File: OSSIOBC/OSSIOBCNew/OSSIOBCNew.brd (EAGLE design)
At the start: 94 x 94 mm, 151 parts, among them Q2 NX-3215, U1 PCA9548APWR, U10 MAX6369, U11 OPA4347, U12 TPS73233, U13 SN65HVD11QD, U14 LTC4411, U16 DS3231-L, U17 FM24V02-G, U18 TMP101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

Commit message: New OBC schematic / board file ok
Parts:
- removed C35: 1uF 0805, OSSI:C0805(2012)
- removed U12: TPS73233, OSSI:SOT23-5DBV
- added C42: 10uF, LDO Tantal 16V, OSSI:C1206(3216)-A
- added R75, R76, R77: 0, OSSI:R0603(1608)
- added U$1: OSSILOGORECT, OSSI:OSSILOGORECT1005
- added U15: MCP1700_SOT23, OSSI:SOT23
- C34: value 1uF 0805 -> 10uF, LDO Tantal 16V; device OSSI:C0805(2012) -> OSSI:C1206(3216)-A
- U9: value ADR127BUJZ-REEL7 -> ADR121
- moved R5 29.6 mm to (43.2, 19.0)
- moved R72 29.3 mm to (44.6, 19.0)
- moved C34 7.91 mm to (63.8, 80.9)
- moved R1 2.27 mm to (67.8, 85.0), turned to 0 degrees
- moved C3 1.38 mm to (66.1, 81.8)
- moved R29 0.12 mm to (41.5, 19.0)
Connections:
- new net N$59: C42.2, R75.1
- new net N$62: R76.1, U5.49
- new net N$64: R77.1, U5.50
- net 3.3VOBC: now also C42.1, U15.2; no longer C34.1, R5.2, R72.2, U12.5
- net 3.3VOBC_I2C: now also R5.2, R72.2
- net GND: now also R75.2, U15.1; no longer C35.2, U12.2
- net MUX_A0: now also R76.2; no longer U5.49
- net MUX_A1: now also R77.2; no longer U5.50
- net N$666: now also C34.1, U15.3; no longer C35.1, U12.1, U12.3
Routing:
- net BAT_TEMP: track 0.00 -> 71.2 mm, vias 0 -> 3
- net SUPERCAP_TEMP: track 0.00 -> 69.6 mm, vias 0 -> 3
- net 3.3VOBC: track 529.4 -> 520.6 mm, vias 20 -> 19
- net MUX_A0: track 36.8 -> 29.4 mm
- net N$666: track 15.2 -> 8.95 mm
- net 3.3VOBC_I2C: track 45.1 -> 50.1 mm
- net N$62: track 0.00 -> 4.83 mm
- net MUX_A1: track 33.5 -> 28.8 mm
- net GND: track 152.4 -> 155.7 mm
- net SC_-PFO: track 89.2 -> 86.0 mm
- net N$64: track 0.00 -> 3.11 mm
- net ADC1: track 28.2 -> 30.3 mm
- net SCOUT_-PG: track 88.9 -> 86.9 mm, vias 1 -> 2
- net N$59: track 0.00 -> 1.77 mm
- net VEXT: track 7.66 -> 8.91 mm
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
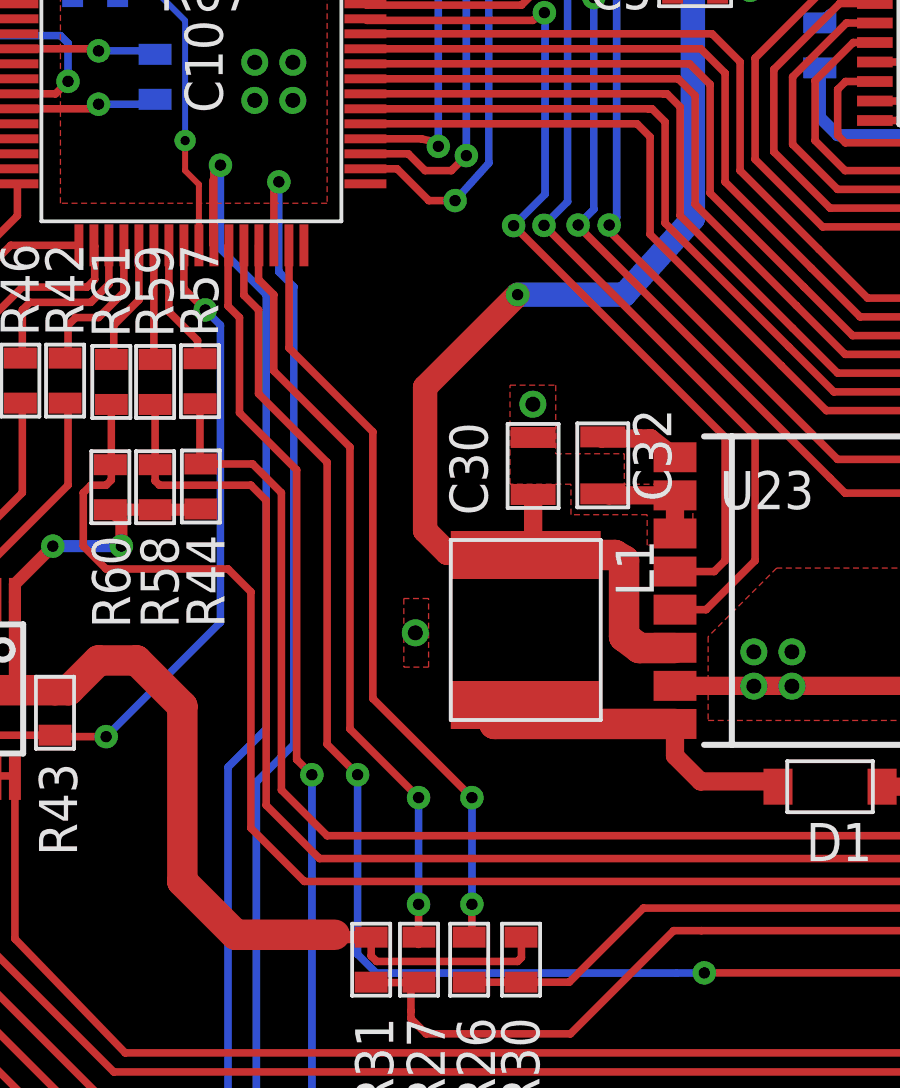
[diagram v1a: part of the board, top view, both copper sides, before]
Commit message: OSSI OBC New Gerber file added
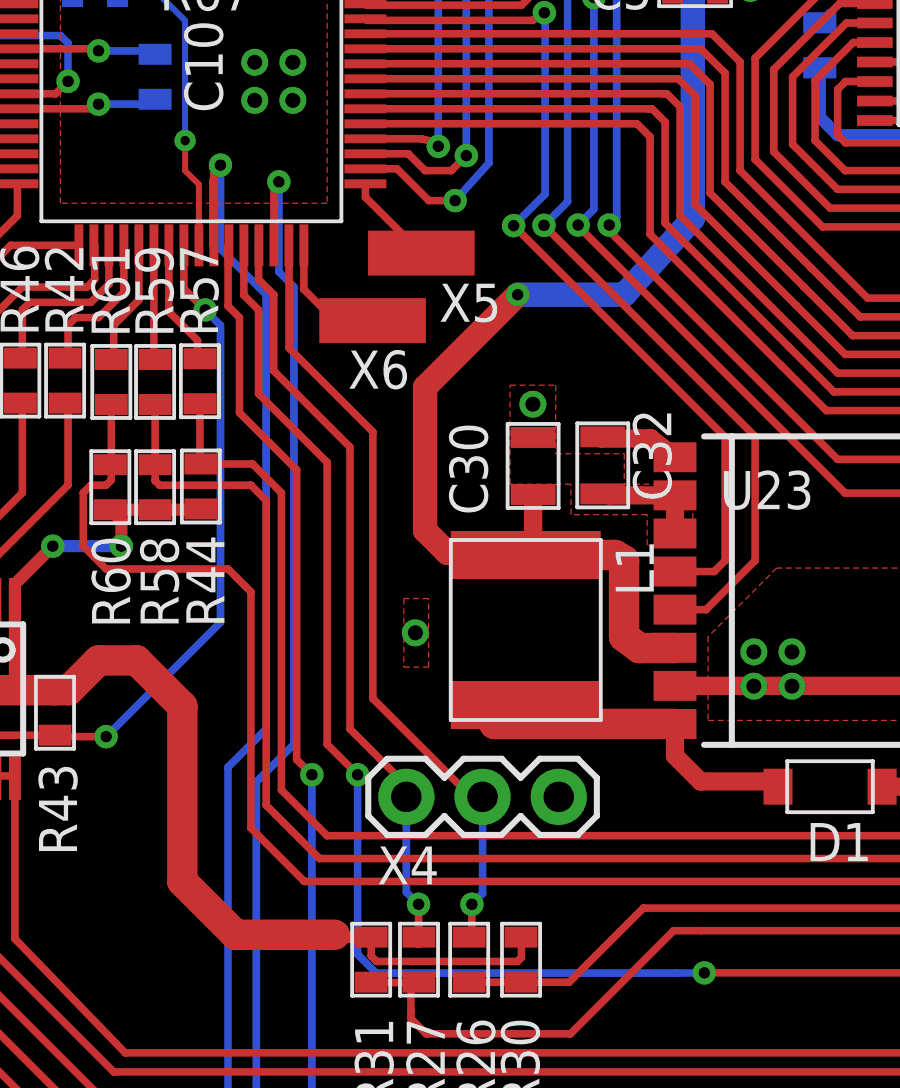
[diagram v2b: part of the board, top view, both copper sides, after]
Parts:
- added X4: (no value), OSSI:1X03
- added X5, X6: P-PAD-S, OSSI:P-PAD-S
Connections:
- new net I2C_SCL_TP: R26.2, U5.31, X4.2
- new net I2C_SDA_TP: R27.2, U5.29, X4.1
- net GND: now also X4.3
- net N$60: now also U5.33, X5.1; no longer R27.2, U5.29
- net N$61: now also U5.32, X6.1; no longer R26.2, U5.31
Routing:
- net I2C_SCL_TP: track 0.00 -> 26.5 mm, vias 0 -> 1
- net I2C_SDA_TP: track 0.00 -> 25.8 mm, vias 0 -> 1
- net N$60: track 25.8 -> 3.08 mm, vias 2 -> 0
- net N$61: track 25.9 -> 4.19 mm, vias 2 -> 0
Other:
- board text added: "A"
- board text added: "B"
- board text added: "GND"
- board text added: "LED"
- board text added: "SCL"
- board text added: "SDA"
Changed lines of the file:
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@@
 <layer number="19" name="Unrouted" color="6" fill="1" visible="yes" active="yes"/>
 <layer number="20" name="Dimension" color="15" fill="1" visible="yes" active="yes"/>
-<layer number="21" name="tPlace" color="7" fill="1" visible="yes" active="yes"/>
-<layer number="22" name="bPlace" color="7" fill="1" visible="yes" active="yes"/>
-<layer number="23" name="tOrigins" color="15" fill="1" visible="yes" active="yes"/>
-<layer number="24" name="bOrigins" color="15" fill="1" visible="yes" active="yes"/>
-<layer number="25" name="tNames" color="7" fill="1" visible="yes" active="yes"/>
-<layer number="26" name="bNames" color="7" fill="1" visible="yes" active="yes"/>
+<layer number="21" name="tPlace" color="7" fill="1" visible="no" active="yes"/>
+<layer number="22" name="bPlace" color="7" fill="1" visible="no" active="yes"/>
+<layer number="23" name="tOrigins" color="15" fill="1" visible="no" active="yes"/>
+<layer number="24" name="bOrigins" color="15" fill="1" visible="no" active="yes"/>
+<layer number="25" name="tNames" color="7" fill="1" visible="no" active="yes"/>
+<layer number="26" name="bNames" color="7" fill="1" visible="no" active="yes"/>
 <layer number="27" name="tValues" color="7" fill="1" visible="no" active="yes"/>
 <layer number="28" name="bValues" color="7" fill="1" visible="no" active="yes"/>
@@
 <layer number="46" name="Milling" color="3" fill="1" visible="no" active="yes"/>
 <layer number="47" name="Measures" color="7" fill="1" visible="no" active="yes"/>
-<layer number="48" name="Document" color="7" fill="1" visible="no" active="yes"/>
+<layer number="48" name="Document" color="7" fill="1" visible="yes" active="yes"/>
 <layer number="49" name="Reference" color="7" fill="1" visible="no" active="yes"/>
 <layer number="50" name="dxf" color="7" fill="1" visible="no" active="no"/>
-<layer number="51" name="tDocu" color="7" fill="1" visible="yes" active="yes"/>
-<layer number="52" name="bDocu" color="7" fill="1" visible="yes" active="yes"/>
+<layer number="51" name="tDocu" color="7" fill="1" visible="no" active="yes"/>
+<layer number="52" name="bDocu" color="7" fill="1" visible="no" active="yes"/>
 <layer number="53" name="tGND_GNDA" color="7" fill="9" visible="no" active="no"/>
 <layer number="54" name="bGND_GNDA" color="1" fill="9" visible="no" active="no"/>
@@
 <wire x1="94" y1="91" x2="91" y2="94" width="0" layer="20" curve="90"/>
 <wire x1="91" y1="94" x2="23" y2="94" width="0" layer="20"/>
-<polygon width="0.4064" layer="37">
-<vertex x="18.375" y="70"/>
-<vertex x="18.375" y="55"/>
-<vertex x="34" y="55"/>
-<vertex x="34" y="70"/>
-</polygon>
-<polygon width="0.4064" layer="37">
-<vertex x="27" y="92.5"/>
-<vertex x="27" y="85.375"/>
-<vertex x="35.25" y="85.375"/>
-<vertex x="35.25" y="92.5"/>
-</polygon>
-<polygon width="0.4064" layer="37">
-<vertex x="55" y="93"/>
-<vertex x="55" y="87"/>
-<vertex x="65" y="87"/>
-<vertex x="65" y="93"/>
-</polygon>
+<rectangle x1="35.5" y1="-0.625" x2="94.5" y2="94" layer="29"/>
+<rectangle x1="26.625" y1="92.625" x2="35.5" y2="94" layer="29"/>
+<rectangle x1="-1.625" y1="74.375" x2="26.625" y2="94" layer="29"/>
+<rectangle x1="25.125" y1="74.125" x2="39.125" y2="85.125" layer="29"/>
+<rectangle x1="-1.75" y1="70.25" x2="37" y2="74.875" layer="29"/>
+<rectangle x1="34.125" y1="47.5" x2="40" y2="71.75" layer="29"/>
+<rectangle x1="-0.375" y1="-0.75" x2="36.75" y2="54.875" layer="29"/>
+<rectangle x1="-1.625" y1="54.25" x2="18.125" y2="70.25" layer="29"/>
+<rectangle x1="26.375" y1="92.625" x2="27" y2="94" layer="29"/>
+<text x="39.625" y="86.125" size="1.016" layer="48" font="vector" rot="R90">GND</text>
+<text x="37.125" y="86.125" size="1.016" layer="48" font="vector" rot="R90">LED</text>
+<text x="32.875" y="34.5" size="1.016" layer="48" font="vector" rot="R90">SDA</text>
+<text x="35.125" y="34.5" size="1.016" layer="48" font="vector" rot="R90">SCL</text>
+<text x="37.75" y="34.5" size="1.016" layer="48" font="vector" rot="R90">GND</text>
+<circle x="21" y="67" radius="0.125" width="0.4064" layer="48"/>
+<circle x="11" y="71.625" radius="0.125" width="0.4064" layer="48"/>
+<circle x="7.125" y="61.375" radius="0.125" width="0.4064" layer="48"/>
+<circle x="21.375" y="44.125" radius="0.125" width="0.4064" layer="48"/>
+<circle x="43.125" y="51.375" radius="0.125" width="0.4064" layer="48"/>
+<circle x="64.625" y="53.875" radius="0.125" width="0.4064" layer="48"/>
+<circle x="64.625" y="63.875" radius="0.125" width="0.4064" layer="48"/>
+<circle x="64.625" y="72.875" radius="0.125" width="0.4064" layer="48"/>
+<circle x="73.625" y="32.375" radius="0.125" width="0.4064" layer="48"/>
+<circle x="53.125" y="67.75" radius="0.125" width="0.4064" layer="48"/>
+<circle x="53.125" y="59.75" radius="0.125" width="0.4064" layer="48"/>
+<circle x="72.25" y="78.625" radius="0.125" width="0.4064" layer="48"/>
+<circle x="50.25" y="8.625" radius="0.125" width="0.4064" layer="48"/>
+<circle x="44.25" y="8.625" radius="0.125" width="0.4064" layer="48"/>
+<circle x="36.25" y="10.625" radius="0.125" width="0.4064" layer="48"/>
+<circle x="29.25" y="12.5" radius="0.125" width="0.4064" layer="48"/>
+<text x="45.375" y="92" size="1.016" layer="48" font="vector">A</text>
+<text x="47.875" y="92" size="1.016" layer="48" font="vector">B</text>
 </plain>
 <attributes>
@@
 <attribute name="VALUE" x="31.236" y="67.343" size="1.27" layer="27"/>
 </element>
+<element name="X4" library="OSSI" package="1X03" value="" x="33.375" y="38.125" smashed="yes">
+<attribute name="NAME" x="32.4038" y="35.2038" size="1.27" layer="25" font="vector" ratio="10"/>
+<attribute name="VALUE" x="32.105" y="34.95" size="1.27" layer="27"/>
+</element>
+<element name="X5" library="OSSI" package="P-PAD-S" value="P-PAD-S" x="33.875" y="56.25" smashed="yes" rot="R180">
+<attribute name="NAME" x="36.54" y="55.23" size="1.27" layer="25" font="vector" rot="R180"/>
+<attribute name="VALUE" x="36.415" y="58.79" size="1.27" layer="27" rot="R180"/>
+</element>
+<element name="X6" library="OSSI" package="P-PAD-S" value="P-PAD-S" x="32.25" y="54" smashed="yes" rot="R180">
+<attribute name="NAME" x="33.5" y="53" size="1.27" layer="25" font="vector" rot="R180"/>
+<attribute name="VALUE" x="34.79" y="56.54" size="1.27" layer="27" rot="R180"/>
+</element>
 </elements>
 <signals>
@@
 <wire x1="59.525" y1="80.575" x2="59.525" y2="81.525" width="0.6096" layer="1"/>
 <wire x1="59.525" y1="81.525" x2="60" y2="82" width="0.6096" layer="1"/>
+<contactref element="X4" pad="3"/>
 </signal>
 <signal name="3.3VOBC">
@@
 <wire x1="28.46" y1="84.34" x2="28.448" y2="84.328" width="0.254" layer="1"/>
 </signal>
-<signal name="N$60">
+<signal name="I2C_SDA_TP">
 <contactref element="U5" pad="29"/>
 <contactref element="R27" pad="2"/>
@@
 <wire x1="28.956" y1="52.324" x2="31.496" y2="49.784" width="0.254" layer="1"/>
 <wire x1="31.496" y1="49.784" x2="31.496" y2="40.386" width="0.254" layer="1"/>
-<wire x1="31.496" y1="40.386" x2="33.782" y2="38.1" width="0.254" layer="1"/>
-<via x="33.782" y="38.1" extent="1-16" drill="0.381"/>
-<wire x1="33.782" y1="38.1" x2="33.782" y2="34.544" width="0.254" layer="16"/>
 <via x="33.782" y="34.544" extent="1-16" drill="0.381"/>
 <wire x1="33.782" y1="34.544" x2="33.782" y2="33.2079875" width="0.254" layer="1"/>
 <wire x1="33.782" y1="33.2079875" x2="33.7959875" y2="33.448" width="0.254" layer="1"/>
+<contactref element="X4" pad="1"/>
+<wire x1="33.375" y1="38.125" x2="33.375" y2="38.507" width="0.254" layer="1"/>
+<wire x1="33.375" y1="38.507" x2="31.496" y2="40.386" width="0.254" layer="1"/>
+<wire x1="33.375" y1="38.125" x2="33.375" y2="34.951" width="0.254" layer="16"/>
+<wire x1="33.375" y1="34.951" x2="33.782" y2="34.544" width="0.254" layer="16"/>
 </signal>
-<signal name="N$61">
+<signal name="I2C_SCL_TP">
 <contactref element="U5" pad="31"/>
 <contactref element="R26" pad="2"/>
@@
 <wire x1="29.464" y1="53.086" x2="32.258" y2="50.292" width="0.254" layer="1"/>
 <wire x1="32.258" y1="50.292" x2="32.258" y2="41.402" width="0.254" layer="1"/>
-<wire x1="32.258" y1="41.402" x2="35.56" y2="38.1" width="0.254" layer="1"/>
-<via x="35.56" y="38.1" extent="1-16" drill="0.381"/>
-<wire x1="35.56" y1="38.1" x2="35.56" y2="34.544" width="0.254" layer="16"/>
 <via x="35.56" y="34.544" extent="1-16" drill="0.381"/>
 <wire x1="35.56" y1="34.544" x2="35.56" y2="33.286009375" width="0.254" layer="1"/>
 <wire x1="35.56" y1="33.286009375" x2="35.467990625" y2="33.448" width="0.254" layer="1"/>
+<contactref element="X4" pad="2"/>
+<wire x1="35.915" y1="38.125" x2="35.535" y2="38.125" width="0.254" layer="1"/>
+<wire x1="35.535" y1="38.125" x2="32.258" y2="41.402" width="0.254" layer="1"/>
+<wire x1="35.915" y1="38.125" x2="35.915" y2="34.899" width="0.254" layer="16"/>
+<wire x1="35.915" y1="34.899" x2="35.56" y2="34.544" width="0.254" layer="16"/>
 </signal>
 <signal name="I2C_SDA">
@@
 <wire x1="31.25" y1="69.5" x2="31.375" y2="69.375" width="0.254" layer="1"/>
 </signal>
+<signal name="N$60">
+<contactref element="U5" pad="33"/>
+<contactref element="X5" pad="1"/>
+<wire x1="32.009996875" y1="58.560003125" x2="32.009996875" y2="58.115003125" width="0.254" layer="1"/>
+<wire x1="32.009996875" y1="58.115003125" x2="33.875" y2="56.25" width="0.254" layer="1"/>
+</signal>
+<signal name="N$61">
+<contactref element="U5" pad="32"/>
+<contactref element="X6" pad="1"/>
+<wire x1="29.959996875" y1="56.510003125" x2="29.959996875" y2="55.040003125" width="0.254" layer="1"/>
+<wire x1="29.959996875" y1="55.040003125" x2="31" y2="54" width="0.254" layer="1"/>
+<wire x1="31" y1="54" x2="32" y2="54" width="0.254" layer="1"/>
+<wire x1="32" y1="54" x2="32.25" y2="54" width="0.254" layer="1"/>
+</signal>
 </signals>
